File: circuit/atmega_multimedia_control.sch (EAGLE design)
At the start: 4 parts, among them IC1 MEGA8-P

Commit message: updated circuit
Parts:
- added C2: 22p, rcl:C-EU025-025X050
- added C3: 100n, rcl:C-EU025-025X050
- added D1, D2: 3v6, diode:ZENER-DIODEDO34-7
- added R2, R3: 68, rcl:R-EU_0204/7
- added R4: 2k2, rcl:R-EU_0204/7
- added X1: usb, con-berg:PN61729
- C1: value (none) -> 22p
- Q1: value (none) -> 20Mhz
- R1: value (none) -> 100k
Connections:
- new net +5V: C3.2, IC1.AVCC, IC1.VCC@1, R1.2, R4.2, X1.1
- new net GND: C1.1, C2.1, C3.1, D1.A, D2.A, IC1.GND, IC1.GND@1, X1.4
- new net N$1: IC1.PC6(/RESET), R1.1
- new net N$2: C1.2, IC1.PB6(XTAL1/TOSC1), Q1.2
- new net N$3: C2.2, IC1.PB7(XTAL2/TOSC2), Q1.1
- new net N$4: IC1.PD4(XCK/T0), R2.2
- new net N$5: D2.C, R3.1, R4.1, X1.3
- new net N$6: D1.C, R2.1, X1.2
- new net N$7: IC1.PD2(INT0), R3.2
- new net N$8: IC1.PC0(ADC0)
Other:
- moved on the sheet: C1, Q1, R1

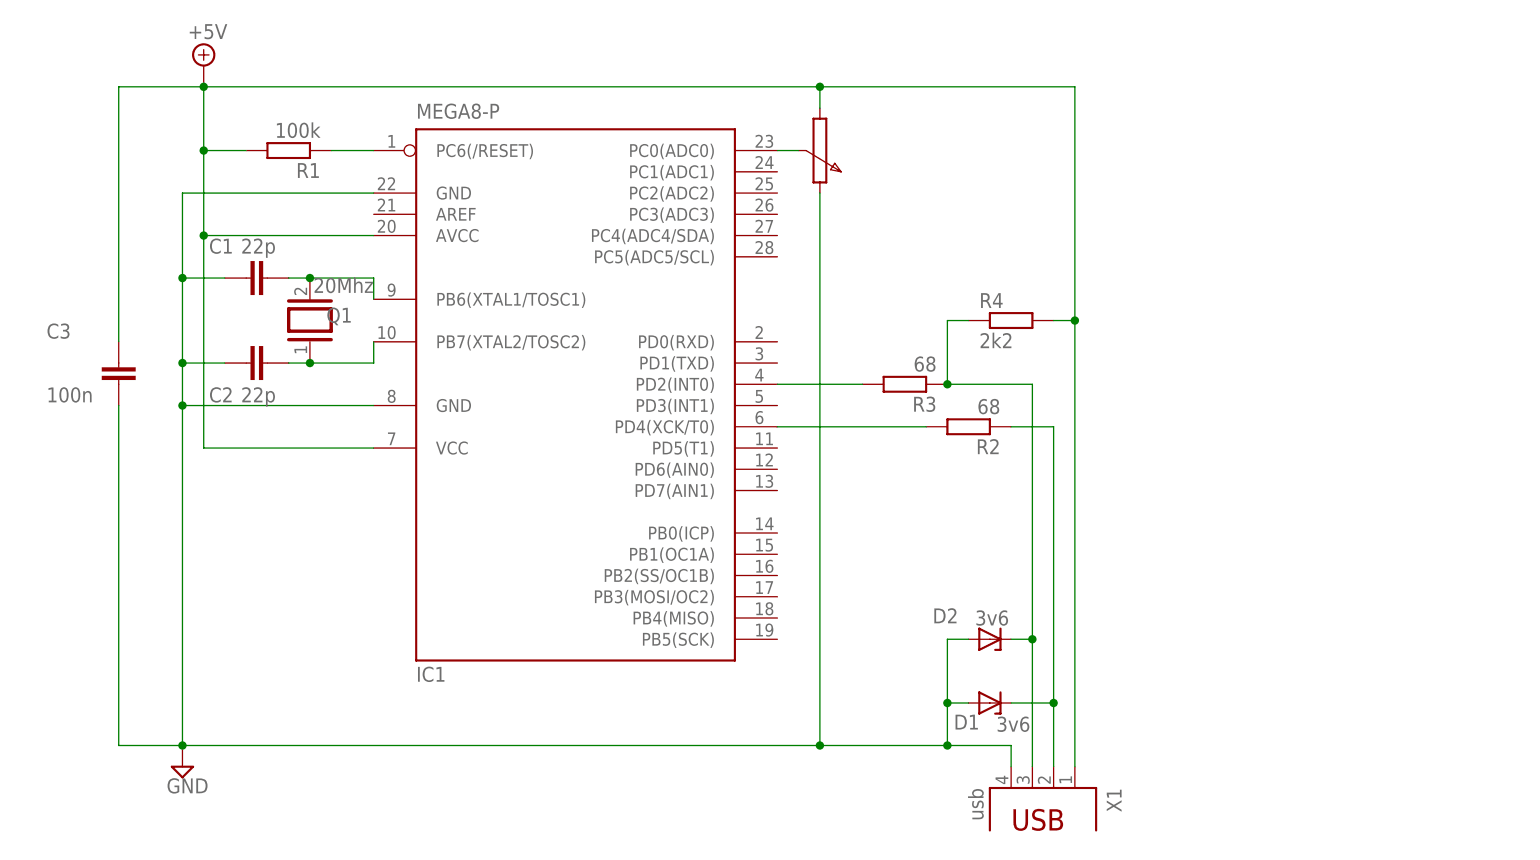
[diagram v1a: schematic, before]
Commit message: circuit and board done
volume knob is missing from board. some led resistors still need proper
placement, will sort that out during soldering
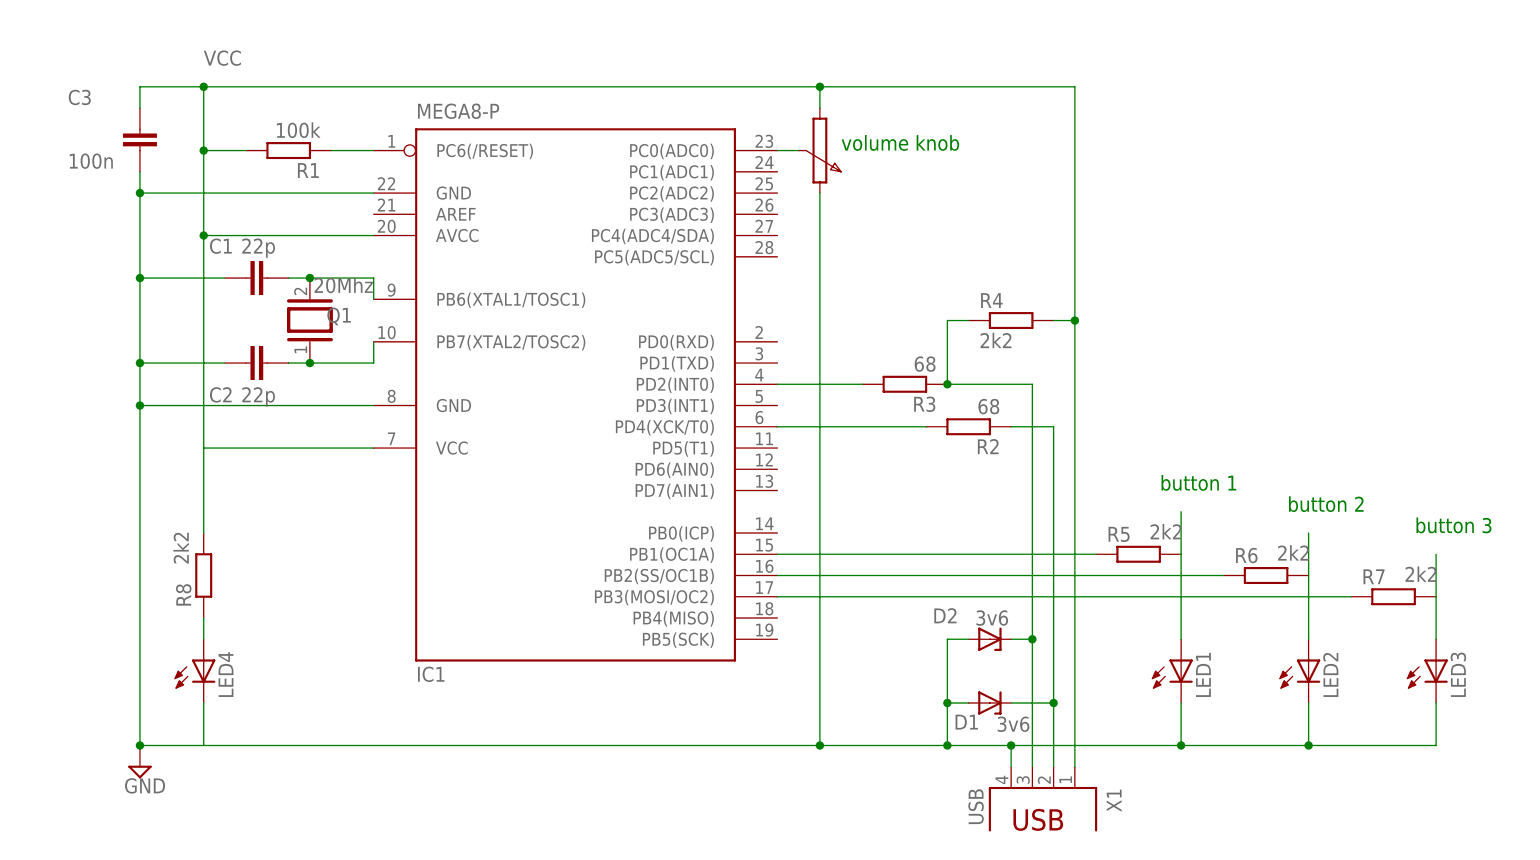
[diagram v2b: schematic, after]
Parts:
- added LED1, LED2, LED3, LED4: (no value), led:LED3MM
- added R5, R6, R7, R8: 2k2, rcl:R-EU_0204/7
- X1: value usb -> USB
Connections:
- removed net +5V: C3.2, IC1.AVCC, IC1.VCC@1, R1.2, R4.2, X1.1
- new net N$10: LED1.A, R5.2
- new net N$11: IC1.PB2(SS/OC1B), R6.1
- new net N$12: LED2.A, R6.2
- new net N$13: IC1.PB3(MOSI/OC2), R7.1
- new net N$14: LED3.A, R7.2
- new net N$15: LED4.A, R8.1
- new net N$9: IC1.PB1(OC1A), R5.1
- new net VCC: C3.2, IC1.AVCC, IC1.VCC@1, R1.2, R4.2, R8.2, X1.1
- net GND: now also LED1.C, LED2.C, LED3.C, LED4.C
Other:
- note added: "button 1"
- note added: "button 2"
- note added: "button 3"
- note added: "volume knob"
- moved on the sheet: C3
